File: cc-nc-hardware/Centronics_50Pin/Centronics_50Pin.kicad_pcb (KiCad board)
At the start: 2 copper layers, 78 x 82.5 mm, 88 parts, among them J1 Conn_01x03_Male, J4 SW, SW1 SW_MEC_5E, U1 SN74CBTD3384, U10 Centronics50PinMale, U2 SN74CBTD3384, U3 AMS1117-2.85, U4 LVT245, U5 LVT125, U6 LVT125, U7 LVT125, U8 74HC14, U9 LVT245

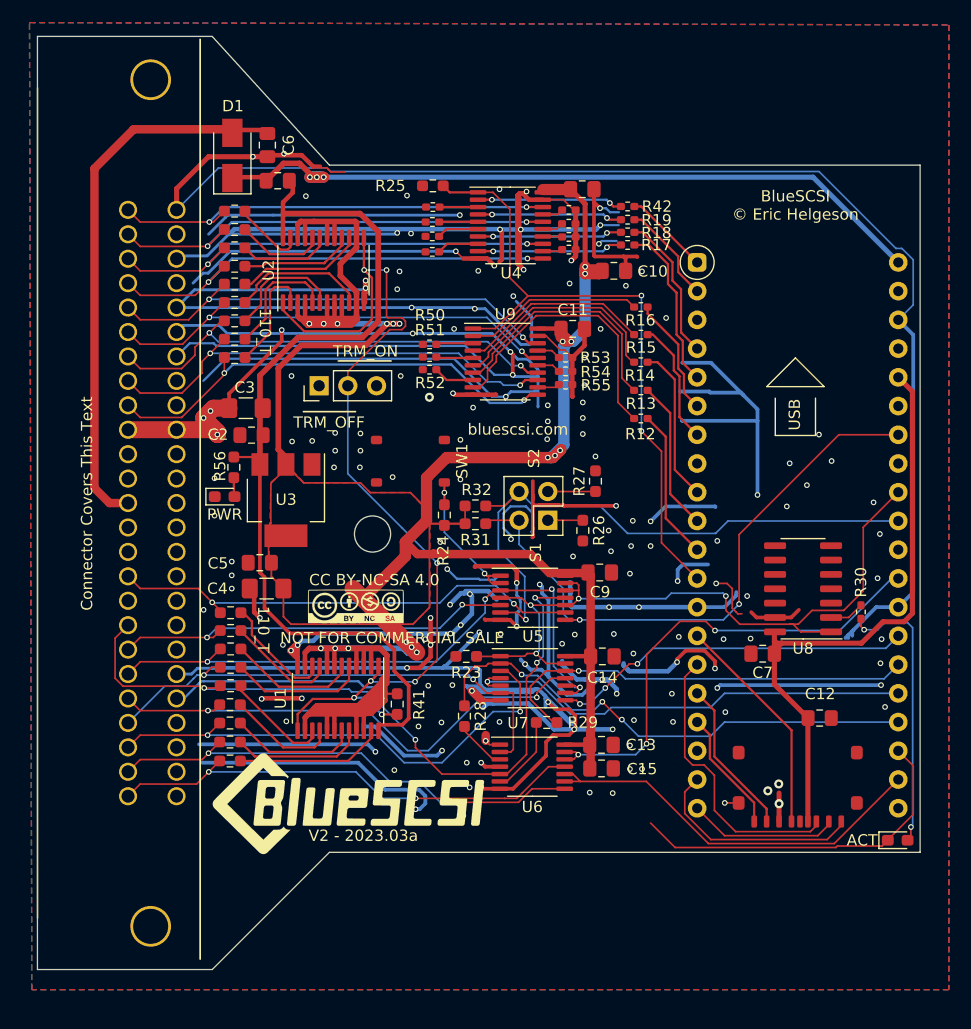
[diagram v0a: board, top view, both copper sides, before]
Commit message: New version of C50, shorter and with options for voltage regulator
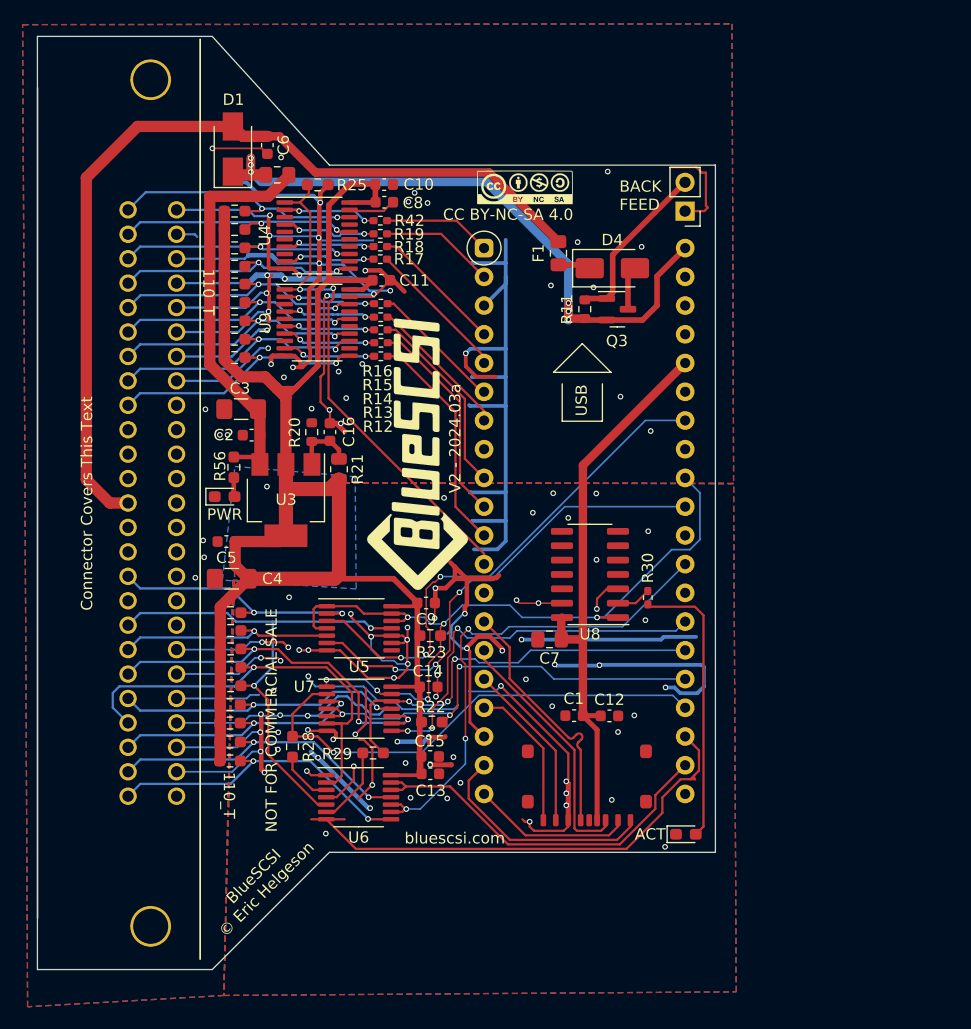
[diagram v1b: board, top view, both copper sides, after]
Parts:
- removed J1: Conn_01x03_Male, Connector_PinHeader_2.54mm:PinHeader_1x03_P2.54mm_Vertical
- removed J4: SW, Connector_PinHeader_2.54mm:PinHeader_2x02_P2.54mm_Vertical
- removed R24, R26, R27: 1k, Resistor_SMD:R_0603_1608Metric_Pad0.98x0.95mm_HandSolder
- removed R31, R32, R41: 4.7k, Resistor_SMD:R_0603_1608Metric_Pad0.98x0.95mm_HandSolder
- removed R43, R44, R45, R46, R47, R48, R49, R50, R51, R52, R53, R54, R55: 1k, Resistor_SMD:R_0402_1005Metric_Pad0.72x0.64mm_HandSolder
- removed REF**: MountingHole_3.2mm_M3, MountingHole:MountingHole_3.2mm_M3
- removed SW1: SW_MEC_5E, Library:TS-1187A-B-A-B
- removed U1, U2: SN74CBTD3384, Package_SO:TSSOP-24_4.4x7.8mm_P0.65mm
- added C1: 0.1uF, Capacitor_SMD:C_0603_1608Metric, F.Cu at (137.0, 119.7)
- added C16: 10uF, Capacitor_SMD:C_0603_1608Metric, F.Cu at (115.4, 94.7)
- added D4: D, Diode_SMD:D_SMA, F.Cu at (140.3, 80.2)
- added F1: Polyfuse, Fuse:Fuse_0805_2012Metric_Pad1.15x1.40mm_HandSolder, F.Cu at (135.6, 78.9)
- added J2: TRM_BCKF, Connector_PinHeader_2.54mm:PinHeader_1x02_P2.54mm_Vertical, F.Cu at (146.8, 75.1)
- added Q3: AO3401A, Package_TO_SOT_SMD:SOT-23, F.Cu at (140.8, 83.8)
- added R20: 154, Resistor_SMD:R_0603_1608Metric, F.Cu at (113.8, 94.7)
- added R21: 120, Resistor_SMD:R_0805_2012Metric, F.Cu at (116.2, 98.0)
- added R22: 4.7k, Resistor_SMD:R_0603_1608Metric_Pad0.98x0.95mm_HandSolder, F.Cu at (124.4, 120.3)
- C10, C11, C13, C14, C15, C8, C9: footprint Capacitor_SMD:C_0805_2012Metric_Pad1.18x1.45mm_HandSolder -> Capacitor_SMD:C_0603_1608Metric
- C12, C2, C5, C6: footprint Capacitor_SMD:C_0805_2012Metric_Pad1.15x1.40mm_HandSolder -> Capacitor_SMD:C_0603_1608Metric
- C4: value 20uF -> 47uF
- R1, R10, R2, R3, R33, R34, R35, R36, R37, R38, R39, R4, R40, R5, R6, R7, R8, R9: value R -> 110
- R11: value 1k -> 10k; footprint Resistor_SMD:R_0402_1005Metric_Pad0.72x0.64mm_HandSolder -> Resistor_SMD:R_0603_1608Metric
- R23, R25: value 1k -> 4.7k
- U3: value AMS1117-2.85 -> AP1117-ADJ
- U4, U9: value LVT245 -> LVTH245
- moved G*** 39.9 mm to (132.6, 73.0)
- moved R12 23.6 mm to (119.9, 88.0)
- moved R13 23.4 mm to (119.9, 86.8)
- moved R14 23.2 mm to (119.9, 85.6)
- moved R15 23.1 mm to (119.8, 84.5)
- moved R16 23.0 mm to (119.9, 83.3)
- moved R17 21.9 mm to (119.8, 79.4)
- moved R18 21.9 mm to (119.8, 78.3)
- moved R19 21.9 mm to (119.8, 77.1)
- moved R42 21.9 mm to (119.8, 76.0)
- moved C10 21.7 mm to (120.2, 72.8)
- moved C7 18.9 mm to (134.8, 113.0)
- moved R30 18.9 mm to (143.5, 109.3)
- moved RP1 18.9 mm to (136.6, 75.9)
- moved U8 18.9 mm to (138.3, 107.3)
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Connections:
- R1 pad 1: Net-(R1-Pad1) -> DB5
- R1 pad 2: DB5 -> +2V8
- R10 pad 1: Net-(R10-Pad1) -> BSY
- R10 pad 2: BSY -> +2V8
- R11 pad 1: GND -> Net-(J2-Pin_2)
- R11 pad 2: Net-(R11-Pad2) -> +5VP
- R2 pad 1: Net-(R2-Pad1) -> ATN
- R2 pad 2: ATN -> +2V8
- R23 pad 2: GND -> +2V8
- R3 pad 1: Net-(R3-Pad1) -> ACK
- R3 pad 2: ACK -> +2V8
- R33 pad 1: Net-(R33-Pad1) -> DB6
- R33 pad 2: DB6 -> +2V8
- R34 pad 1: Net-(R34-Pad1) -> DB7
- R34 pad 2: DB7 -> +2V8
- R35 pad 1: Net-(R35-Pad1) -> DBP
- R35 pad 2: DBP -> +2V8
- R36 pad 1: Net-(R36-Pad1) -> DB0
- R36 pad 2: DB0 -> +2V8
- R37 pad 1: Net-(R37-Pad1) -> DB1
- R37 pad 2: DB1 -> +2V8
- R38 pad 1: Net-(R38-Pad1) -> DB2
- R38 pad 2: DB2 -> +2V8
- R39 pad 1: Net-(R39-Pad1) -> DB3
- R39 pad 2: DB3 -> +2V8
- R4 pad 1: Net-(R4-Pad1) -> RST
- R4 pad 2: RST -> +2V8
- R40 pad 1: Net-(R40-Pad1) -> DB4
- R40 pad 2: DB4 -> +2V8
- R5 pad 1: Net-(R5-Pad1) -> SEL
- R5 pad 2: SEL -> +2V8
- R6 pad 1: Net-(R6-Pad1) -> IO
- R6 pad 2: IO -> +2V8
- R7 pad 1: Net-(R7-Pad1) -> REQ
- R7 pad 2: REQ -> +2V8
- R8 pad 1: Net-(R8-Pad1) -> CD
- R8 pad 2: CD -> +2V8
- R9 pad 1: Net-(R9-Pad1) -> MSG
- R9 pad 2: MSG -> +2V8
- U3 pad 1: GND -> Net-(U3-ADJ)
- U4 pad 12: Net-(R49-Pad1) -> unconnected-(U4-B7-Pad12)
- U4 pad 14: Net-(R48-Pad1) -> unconnected-(U4-B5-Pad14)
- U4 pad 15: Net-(R47-Pad1) -> unconnected-(U4-B4-Pad15)
- U4 pad 17: Net-(R46-Pad1) -> unconnected-(U4-B2-Pad17)
- U4 pad 3: Net-(R11-Pad2) -> unconnected-(U4-A2-Pad3)
- U4 pad 5: Net-(R43-Pad2) -> unconnected-(U4-A4-Pad5)
- U4 pad 6: Net-(R44-Pad2) -> unconnected-(U4-A5-Pad6)
- U4 pad 8: Net-(R45-Pad2) -> unconnected-(U4-A7-Pad8)
- U5 pad 1: oRST -> oBSY
- U5 pad 10: oBSY -> GND
- U5 pad 2: oRST -> ATN
- U5 pad 3: RST -> iATN
- U5 pad 8: iATN -> unconnected-(U5-3Y-Pad8)
- U5 pad 9: ATN -> GND
- U6 pad 10: oREQ -> oIO
- U6 pad 11: IO -> REQ
- U6 pad 12: oIO -> oREQ
- U6 pad 13: oIO -> oREQ
- U6 pad 8: REQ -> IO
- U6 pad 9: oREQ -> oIO
- U9 pad 12: Net-(R55-Pad1) -> unconnected-(U9-B7-Pad12)
- U9 pad 15: Net-(R54-Pad1) -> unconnected-(U9-B4-Pad15)
- U9 pad 17: Net-(R53-Pad1) -> unconnected-(U9-B2-Pad17)
- U9 pad 3: Net-(R50-Pad2) -> unconnected-(U9-A2-Pad3)
- U9 pad 5: Net-(R51-Pad2) -> unconnected-(U9-A4-Pad5)
- U9 pad 8: Net-(R52-Pad2) -> unconnected-(U9-A7-Pad8)
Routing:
- net GND: track 891.9 -> 540.7 mm, vias 167 -> 118
- net +2V8: track 342.5 -> 152.8 mm, vias 19 -> 0
- net TRM_ON_J: track 83.0 -> 0.00 mm, vias 7 -> 0
- net +5F: track 81.4 -> 35.9 mm
- net RST: track 55.9 -> 34.5 mm, vias 4 -> 3
- net +5V: track 57.9 -> 79.1 mm
- net CD: track 44.2 -> 23.1 mm
- net BSY: track 65.1 -> 45.7 mm, vias 4 -> 2
- net ATN: track 42.3 -> 22.9 mm
- net DB7: track 41.8 -> 23.2 mm
- net DB6: track 41.6 -> 23.0 mm
- net DBP: track 41.8 -> 23.3 mm
- net DB3: track 40.4 -> 22.2 mm
- net MSG: track 44.7 -> 26.5 mm
- net DB2: track 40.2 -> 22.0 mm
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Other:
- board size 78 x 82.5 mm -> 59.9 x 82.5 mm
- board text added: "BACK FEED"
- board text added: "V2 - 2024.03a"
- board text added: "© 2023 Tech by Androda, LLC Licensed Attribution-NonCommercial-ShareAlike 4.0 International (CC BY-NC-SA 4.0) https://creativecommons.org/licenses/by-nc-sa/4.0/legalcode"
- board text removed: "S1"
- board text removed: "S2"
- board text removed: "TRM_OFF"
- board text removed: "TRM_ON"
- board text removed: "V2 - 2023.03a"
